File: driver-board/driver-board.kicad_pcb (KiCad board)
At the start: 2 copper layers, 157.7 x 69.9 mm, 27 parts, among them J1 MCP4725, J2 Conn_Coaxial, J3 MCP4725, SW1 RST, U1 Pico, U2 MIC5317, U3 TSV358, U4 TSV358, U5 TCBT-2R5G

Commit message: Passing DRC
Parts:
- added C10: 0.01u, Capacitor_SMD:C_0805_2012Metric_Pad1.18x1.45mm_HandSolder, F.Cu at (123.0, 107.7)
- added C11: 0.1u, Capacitor_SMD:C_0805_2012Metric_Pad1.18x1.45mm_HandSolder, F.Cu at (124.0, 116.0)
- added C12: 100u, Capacitor_THT:CP_Radial_D10.0mm_P3.50mm, F.Cu at (134.9, 124.1)
- added C13: 1u, Capacitor_SMD:C_0805_2012Metric_Pad1.18x1.45mm_HandSolder, F.Cu at (100.0, 109.0)
- added C14: 1u, Capacitor_SMD:C_0805_2012Metric_Pad1.18x1.45mm_HandSolder, F.Cu at (99.0, 116.0)
- added C15: 22p, Capacitor_SMD:C_0805_2012Metric_Pad1.18x1.45mm_HandSolder, F.Cu at (94.5, 124.5)
- added C16: 1u, Capacitor_SMD:C_0805_2012Metric_Pad1.18x1.45mm_HandSolder, F.Cu at (95.5, 120.0)
- added J4: Conn_Coaxial, lib:CONSMA020.062-G, F.Cu at (140.0, 112.5)
- added JP1: SolderJumper_2_Open, Jumper:SolderJumper-2_P1.3mm_Bridged_Pad1.0x1.5mm, F.Cu at (98.0, 99.0)
- added L1: 22u, Inductor_SMD:L_1210_3225Metric_Pad1.42x2.65mm_HandSolder, F.Cu at (99.5, 112.5)
- added L2: 22u, Inductor_SMD:L_1210_3225Metric_Pad1.42x2.65mm_HandSolder, F.Cu at (105.0, 121.0)
- added R3: 1k, Resistor_SMD:R_0805_2012Metric_Pad1.20x1.40mm_HandSolder, F.Cu at (124.0, 111.9)
- added R4: 470k, Resistor_SMD:R_0805_2012Metric_Pad1.20x1.40mm_HandSolder, F.Cu at (97.0, 124.5)
- added R5: 18k, Resistor_SMD:R_0805_2012Metric_Pad1.20x1.40mm_HandSolder, F.Cu at (100.5, 123.0)
- added R7: 0, Resistor_SMD:R_0805_2012Metric_Pad1.20x1.40mm_HandSolder, F.Cu at (108.1, 106.2)
- added R8: 0, Resistor_SMD:R_0805_2012Metric_Pad1.20x1.40mm_HandSolder, F.Cu at (110.0, 110.0)
- added RV2: 100K, lib:PT15-RV15, F.Cu at (115.0, 121.0)
- added SW2: SW_DPDT_x2, lib:JS202011SCQN, F.Cu at (130.5, 106.7)
- added TP5: TestPoint, TestPoint:TestPoint_Pad_D1.5mm, F.Cu at (104.9, 112.8)
- added TP6: TestPoint, TestPoint:TestPoint_Pad_D1.5mm, F.Cu at (104.1, 106.2)
- added TP7: TestPoint, TestPoint:TestPoint_Pad_D1.5mm, F.Cu at (114.0, 111.0)
- added U6: LM2904, Package_SO:TSSOP-8_4.4x3mm_P0.65mm, F.Cu at (116.0, 107.0)
- added U7: LT3462A, Package_TO_SOT_SMD:TSOT-23-6, F.Cu at (100.0, 119.5)
- J1, J3, SW1: moved to F.Cu
- R6: renamed from JP1; value SolderJumper_2_Open -> 0; footprint Jumper:SolderJumper-2_P1.3mm_Bridged_RoundedPad1.0x1.5mm -> Resistor_SMD:R_0805_2012Metric_Pad1.20x1.40mm_HandSolder
- moved SW1 34.6 mm to (62.5, 100.8), turned to -90 degrees
- moved TP4 33.6 mm to (100.7, 93.7)
- moved J2 29.1 mm to (128.1, 75.0)
- moved TP1 29.1 mm to (95.8, 81.9)
- moved LD1 27.7 mm to (139.7, 84.6)
- moved TP3 26.8 mm to (109.0, 103.0), turned to -90 degrees
- moved U5 25.9 mm to (127.8, 88.0), turned to 0 degrees
- moved C5 25.9 mm to (125.8, 86.4)
- moved C6 25.2 mm to (116.5, 99.0)
- moved C7 25.2 mm to (112.9, 99.0)
- moved R2 25.2 mm to (109.5, 99.0)
- moved C4 24.8 mm to (104.7, 93.7)
- moved U4 24.8 mm to (103.4, 99.0)
- moved C8 21.0 mm to (107.4, 80.1), turned to 180 degrees
- moved RN1 20.4 mm to (99.9, 86.0)
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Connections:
- R6 pad 1: DAC_OUT_TIA -> Net-(R6-Pad1)
- R6 pad 2: Net-(JP1-Pad2) -> Net-(R6-Pad2)
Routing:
- net DAC_OUT_TIA: track 138.6 -> 48.6 mm
- net 3V3: track 0.00 -> 64.3 mm, vias 0 -> 2
- net GND: track 18.5 -> 60.1 mm, vias 84 -> 52
- net SiPM Bias: track 0.00 -> 29.5 mm
- net TIA_OUT: track 59.1 -> 33.6 mm
- net 5V: track 46.6 -> 69.0 mm, vias 0 -> 1
- net (no net): track 21.7 -> 0.00 mm, vias 2 -> 0
- net Net-(RV2-Pad2): track 0.00 -> 19.7 mm, vias 0 -> 2
- net Net-(C10-Pad2): track 0.00 -> 14.3 mm
- net A3V3: track 53.0 -> 39.7 mm, vias 0 -> 9
- net Net-(SW1-Pad1): track 12.2 -> 24.6 mm, vias 1 -> 0
- net DAC_OUT_I_SRC: track 43.3 -> 32.8 mm, vias 0 -> 1
- net PD: track 52.6 -> 42.6 mm, vias 1 -> 0
- net Net-(R6-Pad1): track 0.00 -> 9.10 mm
- net Net-(C14-Pad2): track 0.00 -> 8.45 mm
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- added copper zone on F.Cu, net -33V
- added copper zone on F.Cu, net 5V
- added copper zone on B.Cu, net A3V3
- added copper zone on F.Cu, net Net-(C14-Pad1)
- added copper zone on F.Cu, net Net-(C15-Pad1)
- added copper zone on F.Cu, net Net-(R5-Pad1)
- removed copper zone on F.Cu, net 3V3
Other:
- board size 157.7 x 69.9 mm -> 85 x 58 mm

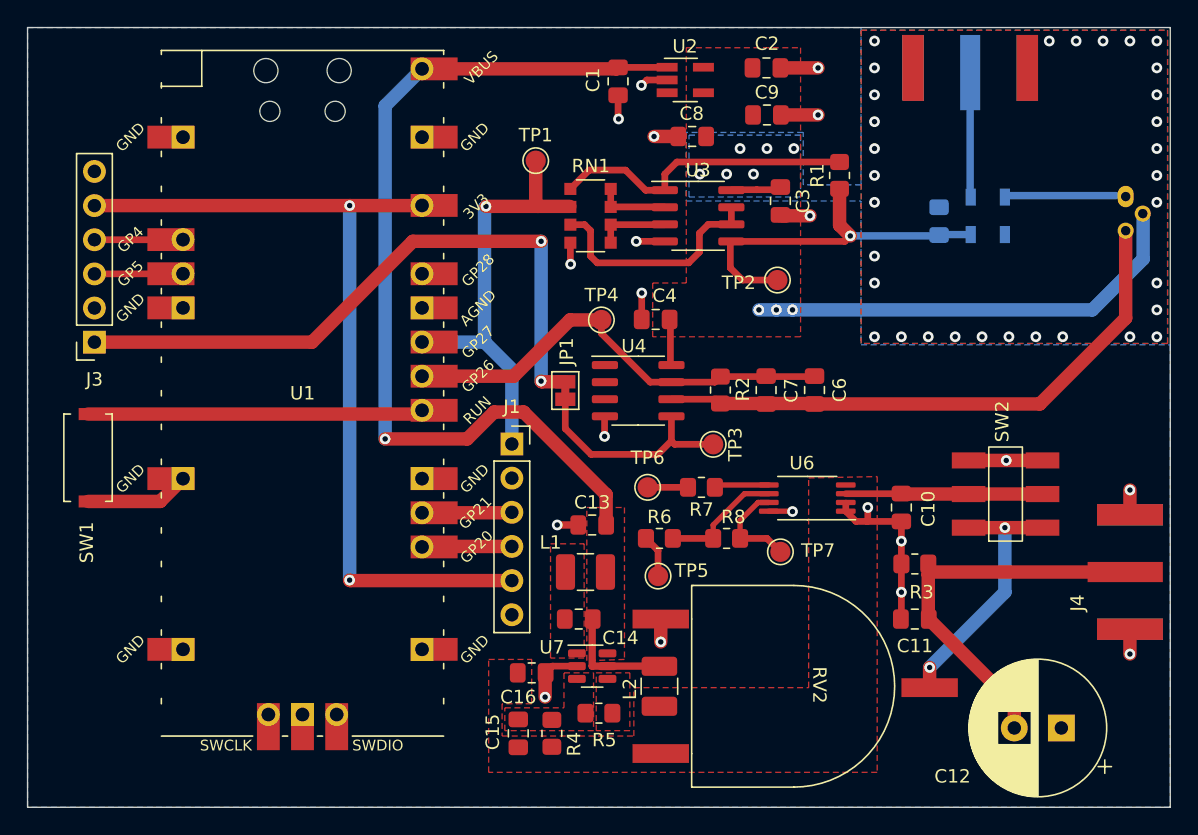
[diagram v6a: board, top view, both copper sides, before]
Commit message: DRC passing, updated HV section and mounting
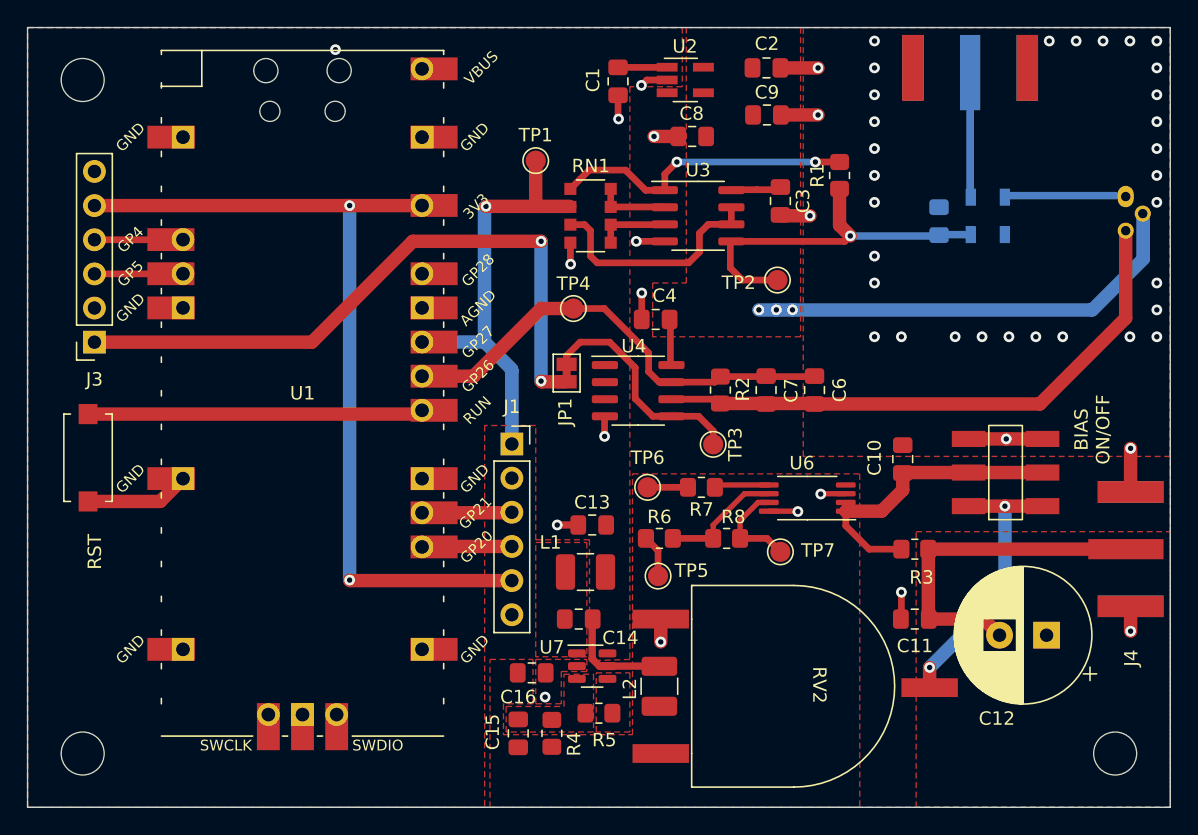
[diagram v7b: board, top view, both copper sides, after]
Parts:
- added REF**: MountingHole_3.2mm_M3, MountingHole:MountingHole_3.2mm_M3, F.Cu at (62.1, 75.9)
- added REF**: MountingHole_3.2mm_M3, MountingHole:MountingHole_3.2mm_M3, F.Cu at (62.1, 126.0)
- added REF**: MountingHole_3.2mm_M3, MountingHole:MountingHole_3.2mm_M3, F.Cu at (138.9, 126.0)
- SW2: value SW_DPDT_x2 -> BIAS ON/OF
- moved C12 6.99 mm to (133.8, 117.2)
- moved C10 3.60 mm to (123.1, 104.1)
- moved TP4 2.25 mm to (98.6, 92.9)
- moved J4 1.70 mm to (140.1, 110.8)
- moved SW2 1.60 mm to (130.5, 105.1)
- moved JP1 1.30 mm to (98.1, 97.7), turned to 90 degrees
- moved R3 1.10 mm to (124.0, 110.8)
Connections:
- C10 pad 1: GND -> Net-(R3-Pad2)
- C10 pad 2: Net-(C10-Pad2) -> GND
- R3 pad 2: GND -> Net-(R3-Pad2)
- SW2 pad 2: Net-(C10-Pad2) -> Net-(R3-Pad2)
- U4 pad 1: (no net) -> unconnected-(U4-Pad1)
- U4 pad 2: (no net) -> unconnected-(U4-Pad2)
- U4 pad 3: (no net) -> unconnected-(U4-Pad3)
- U6 pad 1: GND -> Net-(R3-Pad2)
- U6 pad 2: GND -> Net-(R3-Pad2)
- U6 pad 3: Net-(C10-Pad2) -> GND
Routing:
- net 5V: track 69.0 -> 3.64 mm, vias 1 -> 0
- net Net-(R3-Pad2): track 0.00 -> 23.1 mm
- net Net-(C10-Pad2): track 14.3 -> 0.00 mm
- net GND: track 60.1 -> 48.2 mm, vias 52 -> 51
- net SiPM Bias: track 29.5 -> 25.6 mm
- net Net-(RV2-Pad2): track 19.7 -> 21.3 mm
- net TIA_OUT: track 33.6 -> 34.5 mm
- net Net-(JP1-Pad2): track 16.3 -> 17.0 mm
- net Net-(R1-Pad2): vias 0 -> 2
- net A3V3: vias 9 -> 3
- added copper zone on F.Cu, net SiPM Bias
- removed copper zone on B.Cu, net A3V3
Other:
- board text added: "BIAS ON/OFF"
- board text added: "Boost Converter -33V"
- board text added: "DAC Current Source"
- board text added: "FD-fNIRS v1 rohit@mendi.io"
- board text added: "RST"
- board text added: "Raspberry Pi Pico"

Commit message: Board reviewed, silk screen fixes
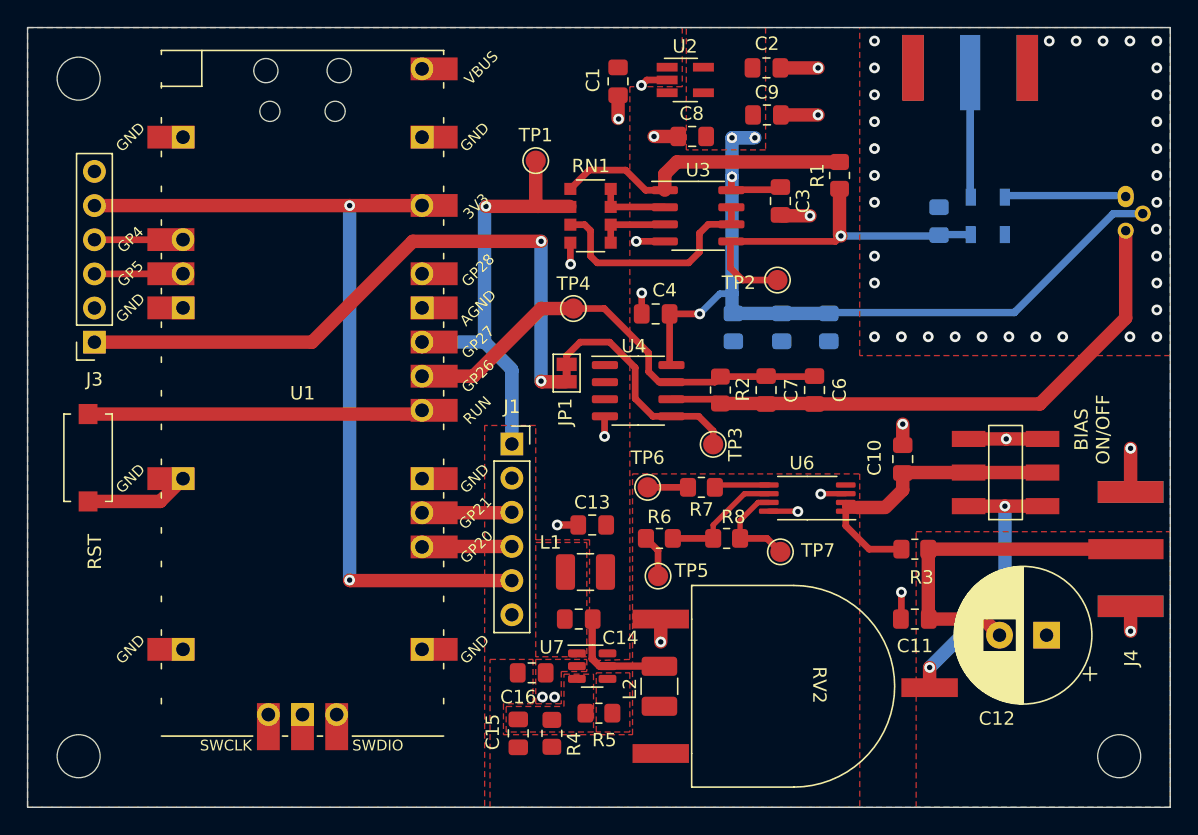
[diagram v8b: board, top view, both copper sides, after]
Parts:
- removed the REF** at (62.1, 75.9)
- removed the REF** at (62.1, 126.0)
- removed the REF** at (138.9, 126.0)
- added C17: 1u, Capacitor_SMD:C_0805_2012Metric_Pad1.18x1.45mm_HandSolder, B.Cu at (114.1, 94.3)
- added C18: 0.1u, Capacitor_SMD:C_0805_2012Metric_Pad1.18x1.45mm_HandSolder, B.Cu at (117.6, 94.3)
- added C19: 0.01u, Capacitor_SMD:C_0805_2012Metric_Pad1.18x1.45mm_HandSolder, B.Cu at (110.5, 94.3)
- added FID1: Logo, lib:mendi-logo-plain, B.Cu at (132.3, 125.2)
- added REF**: MountingHole_3.2mm_M3, MountingHole:MountingHole_3.2mm_M3, F.Cu at (139.2, 126.2)
- added REF**: MountingHole_3.2mm_M3, MountingHole:MountingHole_3.2mm_M3, F.Cu at (61.8, 126.2)
- added REF**: MountingHole_3.2mm_M3, MountingHole:MountingHole_3.2mm_M3, F.Cu at (61.8, 75.8)
- moved C4 0.41 mm to (104.7, 93.3)
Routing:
- net A3V3: track 39.7 -> 61.8 mm, vias 3 -> 4
- net 5V: track 3.64 -> 0.00 mm
- net GND: track 48.2 -> 49.3 mm, vias 51 -> 55
- net Net-(R1-Pad2): vias 2 -> 0
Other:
- board text added: "-V Bias"
- board text added: "Boost Converter"
- board text added: "Current Source"
- board text added: "FD-fNIRS v1 rohitrathnam.n@gmail.com mendi.io"
- board text added: "TIA"
- board text removed: "Boost Converter -33V"
- board text removed: "FD-fNIRS v1 rohit@mendi.io"
